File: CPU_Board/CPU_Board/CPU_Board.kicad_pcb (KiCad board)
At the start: 2 copper layers, 60 x 100 mm, 102 parts, among them J101 Screw_Terminal_01x03, J102 Conn_02x01, J103 Conn_02x01, J104 Conn_01x08_Male, J105 Conn_02x09_Odd_Even, J106 Micro_SD_Card_Det, J107 Conn_01x06_Male, J108 Conn_02x01, J109 Conn_02x01, J110 Screw_Terminal_01x04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

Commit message: ram verdrahtung nicht optimal - noch mal versuchen
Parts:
- removed J111: Conn_02x09_Odd_Even, Connector_PinHeader_2.54mm:PinHeader_2x09_P2.54mm_Vertical
- added D101: LED_blue, LED_SMD:LED_0603_1608Metric, F.Cu at (72.0, 77.8)
- added D102: LED_red, LED_SMD:LED_0603_1608Metric, F.Cu at (74.5, 77.8)
- added D103: LED_blue, LED_SMD:LED_0603_1608Metric, F.Cu at (79.5, 77.8)
- added D104: LED_blue, LED_SMD:LED_0603_1608Metric, F.Cu at (77.0, 77.8)
- added R120: 1K, Resistor_SMD:R_0603_1608Metric, F.Cu at (72.0, 80.8)
- added R121: 1K, Resistor_SMD:R_0603_1608Metric, F.Cu at (74.5, 80.8)
- added R124: 1K, Resistor_SMD:R_0603_1608Metric, F.Cu at (79.5, 80.8)
- added R133: 1K, Resistor_SMD:R_0603_1608Metric, F.Cu at (77.0, 80.8)
- moved J106 55.1 mm to (126.9, 136.4), turned to 90 degrees
- moved C122 46.5 mm to (71.5, 125.7), turned to 90 degrees
- moved C129 33.1 mm to (91.3, 131.0), turned to 315 degrees
- moved C132 32.6 mm to (78.9, 119.3), turned to 90 degrees
- moved U102 32.2 mm to (83.9, 126.3), turned to 315 degrees
- moved R111 30.9 mm to (101.1, 114.8), turned to 270 degrees
- moved R125 29.5 mm to (113.1, 136.3), turned to 90 degrees
- moved C125 27.6 mm to (80.9, 116.5), turned to 90 degrees
- moved C130 27.3 mm to (94.5, 127.8), turned to 315 degrees
- moved R123 27.2 mm to (113.2, 125.6), turned to 90 degrees
- moved R114 26.8 mm to (111.6, 136.3), turned to 270 degrees
- moved C142 26.7 mm to (113.5, 130.7), turned to 270 degrees
- moved R122 24.3 mm to (111.7, 125.6), turned to 90 degrees
- moved R117 24.3 mm to (110.0, 136.3), turned to 270 degrees
- moved C123 22.2 mm to (83.9, 113.5), turned to 90 degrees
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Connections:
- U101 pad 101: /PA9 -> (no net)
- U101 pad 110: /PA15 -> (no net)
- U101 pad 111: /PC10 -> (no net)
- U101 pad 112: /PC11 -> (no net)
- U101 pad 113: /PC12 -> (no net)
- U101 pad 116: /PD2 -> (no net)
- U101 pad 118: /PD4 -> (no net)
- U101 pad 119: /PD5 -> (no net)
- U101 pad 122: /PD6 -> (no net)
- U101 pad 123: /PD7 -> (no net)
- U101 pad 134: /PB4 -> (no net)
- U101 pad 137: /PB7 -> (no net)
- U101 pad 139: /PB8 -> (no net)
- U101 pad 140: /PB9 -> (no net)
- U101 pad 18: /PF6 -> (no net)
- U101 pad 19: /PF7 -> (no net)
- U101 pad 20: /PF8 -> (no net)
- U101 pad 21: /PF9 -> (no net)
- U101 pad 22: /PF10 -> (no net)
- U101 pad 28: /PC2 -> (no net)
- U101 pad 29: /PC3 -> (no net)
- U101 pad 37: /PA3 -> (no net)
- U101 pad 44: /PC4 -> (no net)
- U101 pad 45: /PC5 -> (no net)
- U101 pad 47: /PB1 -> (no net)
- U101 pad 48: /PB2 -> (no net)
- U101 pad 73: /PB12 -> (no net)
- U101 pad 80: /PD11 -> (no net)
- U101 pad 81: /PD12 -> (no net)
- U101 pad 82: /PD13 -> (no net)
- U101 pad 87: /PG2 -> (no net)
- U101 pad 88: /PG3 -> (no net)
- U101 pad 9: /PC15 -> (no net)
- U101 pad 91: /PG6 -> (no net)
- U101 pad 92: /PG7 -> (no net)
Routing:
- net /NBL1: track 0.00 -> 65.5 mm, vias 0 -> 2
- net /BA1: track 0.00 -> 58.3 mm, vias 0 -> 2
- net /BA0: track 0.00 -> 56.8 mm, vias 0 -> 2
- net /A4: track 0.00 -> 56.5 mm, vias 0 -> 2
- net /A5: track 0.00 -> 55.0 mm, vias 0 -> 2
- net /NBL0: track 0.00 -> 54.7 mm, vias 0 -> 2
- net /PB5: track 0.00 -> 54.3 mm, vias 0 -> 2
- net /PG8: track 0.00 -> 52.8 mm, vias 0 -> 2
- net /PG15: track 0.00 -> 49.8 mm, vias 0 -> 2
- net /DQ2: track 0.00 -> 48.9 mm, vias 0 -> 2
- net /PB6: track 0.00 -> 48.7 mm, vias 0 -> 2
- net /DQ15: track 0.00 -> 47.8 mm, vias 0 -> 2
- net /DQ14: track 0.00 -> 47.7 mm, vias 0 -> 2
- net /A3: track 0.00 -> 47.7 mm, vias 0 -> 2
- net /A10: track 0.00 -> 47.6 mm, vias 0 -> 2
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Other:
- copper layers 2 -> 4
- net class 50OhmS added: clearance 0.15, trace_width 0.35, via_dia 0.45, via_drill 0.2
- net class Default: clearance 0.2 -> 0.15; trace_width 0.25 -> 0.15; via_dia 0.8 -> 0.45; via_drill 0.4 -> 0.2
- rule trace_clearance: 0.2 -> 0.15
- rule trace_min: 0.2 -> 0.15
- rule via_min_drill: 0.3 -> 0.2
- rule via_min_size: 0.4 -> 0.45
- board text added: "Error"
- board text added: "Status"

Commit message: RAM auf die rückseite verlegt, alles auf 55mm length gematcht
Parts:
- C122, C123, C125, C129, C130, C131, C132, U102: moved to B.Cu
- moved C119 118.4 mm to (200.1, 86.0), turned to 90 degrees
- moved C103 116.9 mm to (200.3, 92.4), turned to 270 degrees
- moved C117 113.7 mm to (197.7, 86.0), turned to 90 degrees
- moved C122 112.7 mm to (183.6, 113.7)
- moved Y101 110.9 mm to (197.3, 92.5), turned to 0 degrees
- moved C102 109.7 mm to (196.9, 95.1), turned to 0 degrees
- moved C107 107.4 mm to (194.5, 86.0), turned to 90 degrees
- moved FB101 105.4 mm to (194.2, 89.9), turned to 270 degrees
- moved C109 102.7 mm to (192.1, 86.0), turned to 90 degrees
- moved C106 100.3 mm to (191.5, 89.0), turned to 0 degrees
- moved R103 99.5 mm to (191.5, 91.2), turned to 0 degrees
- moved C110 98.9 mm to (191.5, 100.8), turned to 0 degrees
- moved C104 98.6 mm to (191.4, 95.2), turned to 0 degrees
- moved C132 94.5 mm to (173.2, 113.8)
- moved C108 92.2 mm to (185.0, 80.9), turned to 90 degrees
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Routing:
- net /NBL0: track 54.7 -> 20.2 mm, vias 2 -> 1
- net /PC0: track 29.9 -> 54.8 mm, vias 2 -> 1
- net /DQ4: track 33.3 -> 54.7 mm, vias 2 -> 1
- net /DQ9: track 35.2 -> 55.1 mm, vias 0 -> 1
- net /DQ11: track 35.3 -> 55.2 mm, vias 2 -> 1
- net /DQ8: track 35.0 -> 54.6 mm, vias 2 -> 1
- net /DQ12: track 35.4 -> 54.8 mm, vias 2 -> 1
- net /DQ10: track 35.6 -> 54.9 mm, vias 2 -> 1
- net +3V3: track 18.9 -> 0.00 mm
- net /PB6: track 48.7 -> 67.1 mm, vias 2 -> 1
- net /PF11: track 36.8 -> 54.4 mm, vias 2 -> 1
- net /DQ5: track 37.7 -> 55.0 mm, vias 0 -> 1
- net /DQ3: track 46.7 -> 63.5 mm, vias 2 -> 1
- net /DQ1: track 40.3 -> 57.0 mm, vias 2 -> 1
- net /DQ6: track 38.9 -> 54.9 mm, vias 0 -> 1
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
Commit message: RAM (55mm) und SDCARD (65 mm) length gematcht, fehlt noch DCMI
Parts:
- added R134: DNP, Resistor_SMD:R_0603_1608Metric, F.Cu at (126.3, 80.4)
- moved C102 80.3 mm to (117.3, 105.4)
- moved C104 80.3 mm to (111.8, 105.5)
- moved C105 80.3 mm to (81.8, 114.0)
- moved C111 80.3 mm to (99.2, 91.1)
- moved C118 80.3 mm to (99.3, 119.8)
- moved C119 80.3 mm to (120.5, 96.3)
- moved C123 80.3 mm to (82.8, 124.1)
- moved C101 80.3 mm to (86.6, 90.5)
- moved C103 80.3 mm to (120.8, 102.7)
- moved C106 80.3 mm to (111.9, 99.3)
- moved C107 80.3 mm to (114.9, 96.2)
- moved C108 80.3 mm to (105.4, 91.2)
- moved C109 80.3 mm to (112.5, 96.2)
- moved C112 80.3 mm to (94.1, 91.4)
- moved C113 80.3 mm to (89.0, 90.9)
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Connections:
- J107 pad 6: /PB3 -> /R_SWO
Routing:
- net /CAM_D2: track 0.00 -> 87.7 mm
- net /CAM_PCLK: track 0.00 -> 80.1 mm
- net /PB14: track 0.00 -> 75.7 mm, vias 0 -> 2
- net /PC1: track 0.00 -> 74.9 mm, vias 0 -> 2
- net /PA0: track 0.00 -> 71.8 mm, vias 0 -> 2
- net /PG12: track 0.00 -> 71.5 mm, vias 0 -> 2
- net /PA1: track 0.00 -> 70.1 mm, vias 0 -> 2
- net /CAM_XCLK: track 0.00 -> 69.8 mm, vias 0 -> 1
- net /PB15: track 0.00 -> 69.2 mm, vias 0 -> 2
- net /PB3: track 0.00 -> 68.4 mm, vias 0 -> 2
- net /CAM_HSYNC: track 0.00 -> 66.5 mm
- net /CAM_D1: track 0.00 -> 64.0 mm
- net /CAM_D0: track 0.00 -> 63.5 mm
- net /CAM_D3: track 0.00 -> 63.1 mm
- net /CAM_VSYNC: track 0.00 -> 46.1 mm, vias 0 -> 1
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
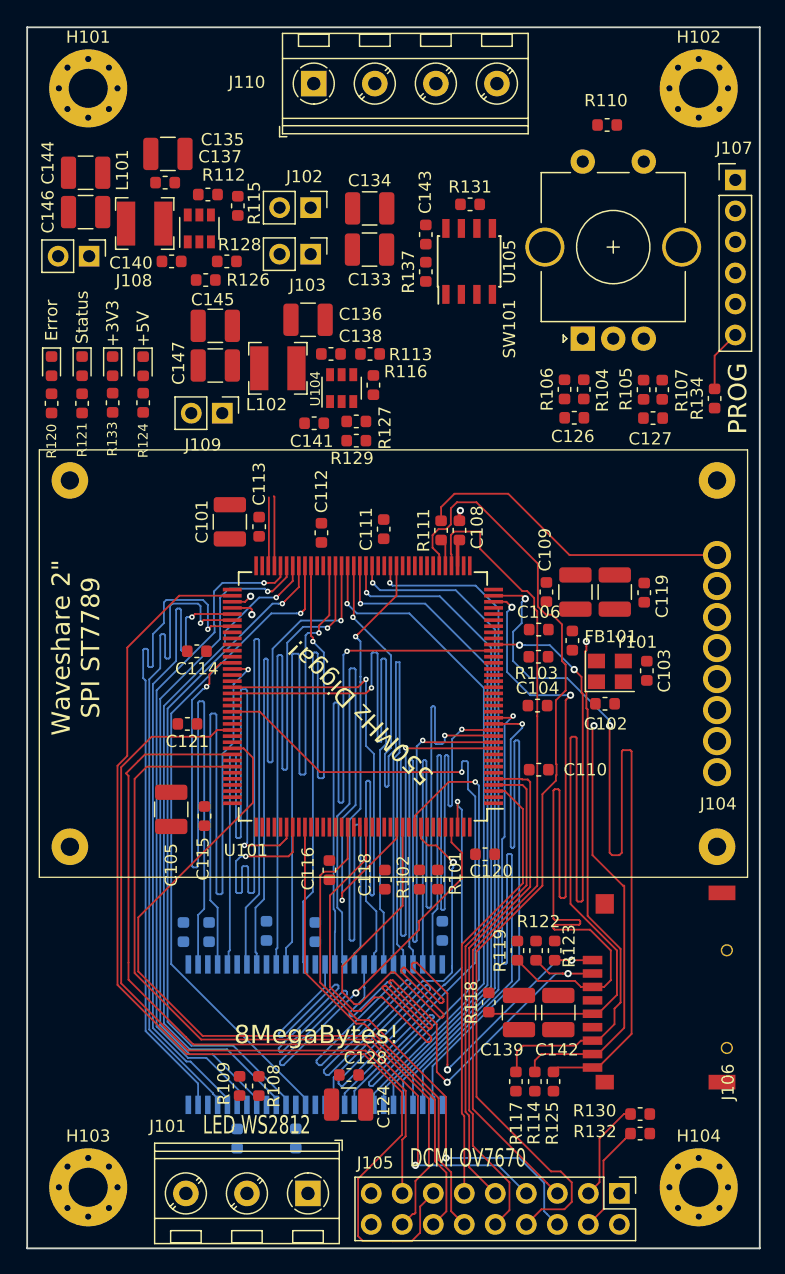
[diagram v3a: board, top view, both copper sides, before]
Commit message: PCB fertig. Length matching RAM 55mm, DCMI 90mm, SD-Card 65mm.. Pins für interfaces erneut mit Evalboard und CubeMX muxtool verglichen
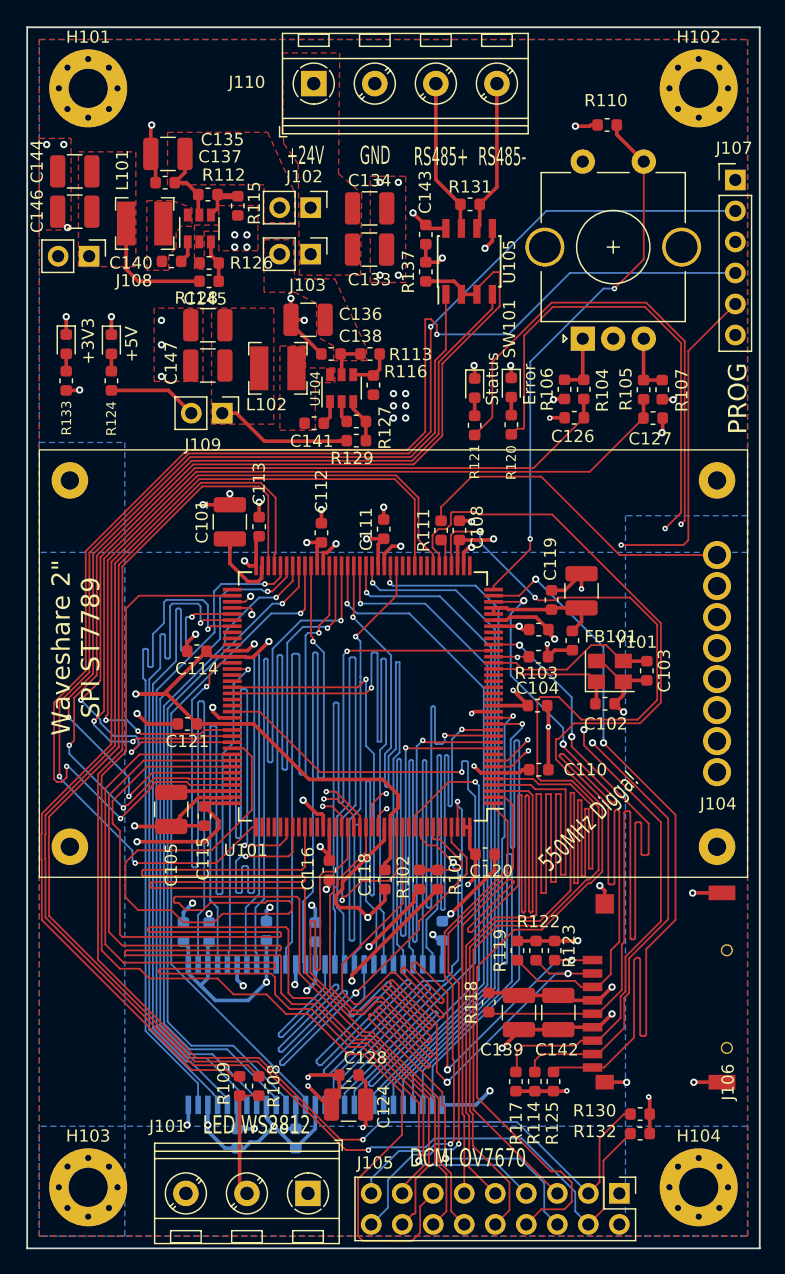
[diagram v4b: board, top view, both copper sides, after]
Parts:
- removed C107: 2.2u, Capacitor_SMD:C_1210_3225Metric
- removed C109: 100n, Capacitor_SMD:C_0603_1608Metric
- removed R134: DNP, Resistor_SMD:R_0603_1608Metric
- C117: value 2.2u -> 10u
- moved D101 37.7 mm to (109.7, 79.5)
- moved R120 37.7 mm to (109.7, 82.5)
- moved D102 32.2 mm to (106.7, 79.5)
- moved R121 32.2 mm to (106.7, 82.6)
- moved C119 7.61 mm to (113.0, 96.9)
- moved D104 4.20 mm to (73.2, 76.0)
- moved R133 4.20 mm to (73.2, 79.0), turned to 90 degrees
- moved D103 3.16 mm to (76.9, 76.0)
- moved R124 3.16 mm to (76.9, 79.0)
- moved C117 2.73 mm to (115.4, 96.2)
- moved R128 2.18 mm to (84.9, 70.8), turned to 180 degrees
- moved R126 1.42 mm to (84.9, 69.3)
- moved C144 0.89 mm to (73.9, 61.8)
- moved C146 0.89 mm to (73.9, 65.1)
- moved C145 0.61 mm to (84.8, 74.4)
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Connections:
- C127 pad 1: /CAM_D0 -> /PC6
- J107 pad 6: /R_SWO -> (no net)
- R105 pad 2: /CAM_D0 -> /PC6
- R109 pad 1: /DISP_DIN -> /PA7
- U101 pad 101: (no net) -> /CAM_D0
- U101 pad 123: (no net) -> /DISP_DIN
- U101 pad 43: /DISP_DIN -> /PA7
- U101 pad 96: /CAM_D0 -> /PC6
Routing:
- net GND: track 0.87 -> 174.8 mm, vias 1 -> 72
- net +3V3: track 2.17 -> 170.7 mm, vias 0 -> 28
- net /PA14: track 0.00 -> 109.7 mm, vias 0 -> 3
- net /PA13: track 0.00 -> 108.2 mm, vias 0 -> 3
- net /CAM_SIOC: track 14.6 -> 118.1 mm, vias 0 -> 1
- net /CAM_SIOD: track 13.9 -> 111.4 mm, vias 0 -> 1
- net /PA7: track 0.00 -> 88.1 mm
- net /PB0: track 0.00 -> 87.8 mm
- net +5V: track 0.00 -> 83.8 mm, vias 0 -> 2
- net /PC8: track 0.00 -> 83.7 mm, vias 0 -> 2
- net /PA12: track 0.00 -> 78.8 mm, vias 0 -> 2
- net /PA11: track 0.00 -> 75.8 mm, vias 0 -> 2
- net /PC6: track 0.00 -> 74.3 mm, vias 0 -> 2
- net /PC14: track 0.00 -> 73.8 mm, vias 0 -> 2
- net /PC7: track 0.00 -> 71.6 mm, vias 0 -> 2
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- added copper zone on F.Cu, net +24V
- added copper zone on In1.Cu, net +3V3
- added copper zone on B.Cu, net GND
- added copper zone on F.Cu, net GND
- added copper zone on In2.Cu, net GND
- added copper zone on F.Cu, net Net-(C135-Pad1)
- added copper zone on F.Cu, net Net-(C136-Pad1)
- added copper zone on F.Cu, net Net-(C140-Pad1)
- added copper zone on F.Cu, net Net-(C141-Pad1)
- added copper zone on F.Cu, net Net-(C144-Pad1)
- added copper zone on F.Cu, net Net-(C145-Pad1)
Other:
- board text added: "+24V"
- board text added: "8MegaBytes! @ 200MHz"
- board text added: "GND"
- board text added: "RS485+"
- board text added: "RS485-"
- board text removed: "8MegaBytes!"
